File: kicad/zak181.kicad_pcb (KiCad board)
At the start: 4 copper layers, 215.3 x 92.7 mm, 119 parts, among them IC1 Z180, J1 JTAG, J10 DE15, J2 DB25_Receptacle_MountingHoles, J3 Compact Flash, J4 Speaker, J5 Keyboard, J7 DSUB-9, J8 USB C, J9 Reset, Q2 BC547, Q3 BC547, Q4 BC547, Q5 BC547, SW1 Reset, U17 LM386, U18 NE555P, U2 Z80 PIO A, U20 XC95108PC84, U21 74HC377, U22 74HC244, U23 27C64, U24 74HC166, U25 MAX232, U26 CH340N, U27 62256, U28 AS6C4008, U29 27C128, U3 AY-3-8912, U30 74HC377, U31 GAL16V8, U32 74HC157, U33 GAL16V8, U40 AS6C4008, U8 74HC138, X1 25.175 MHz, Y2 12.288 MHz

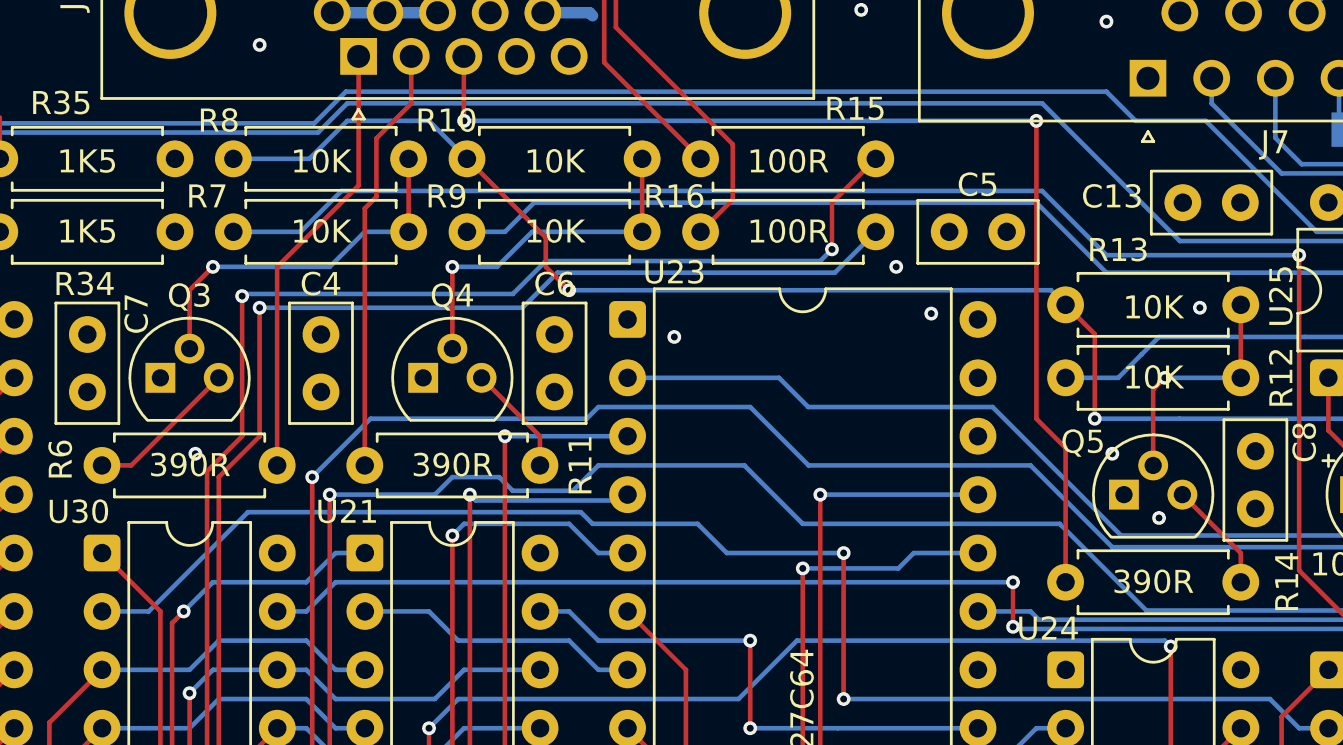
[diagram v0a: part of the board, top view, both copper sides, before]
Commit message: hw/vga: reduce resistance in DAC to impove image sharpness
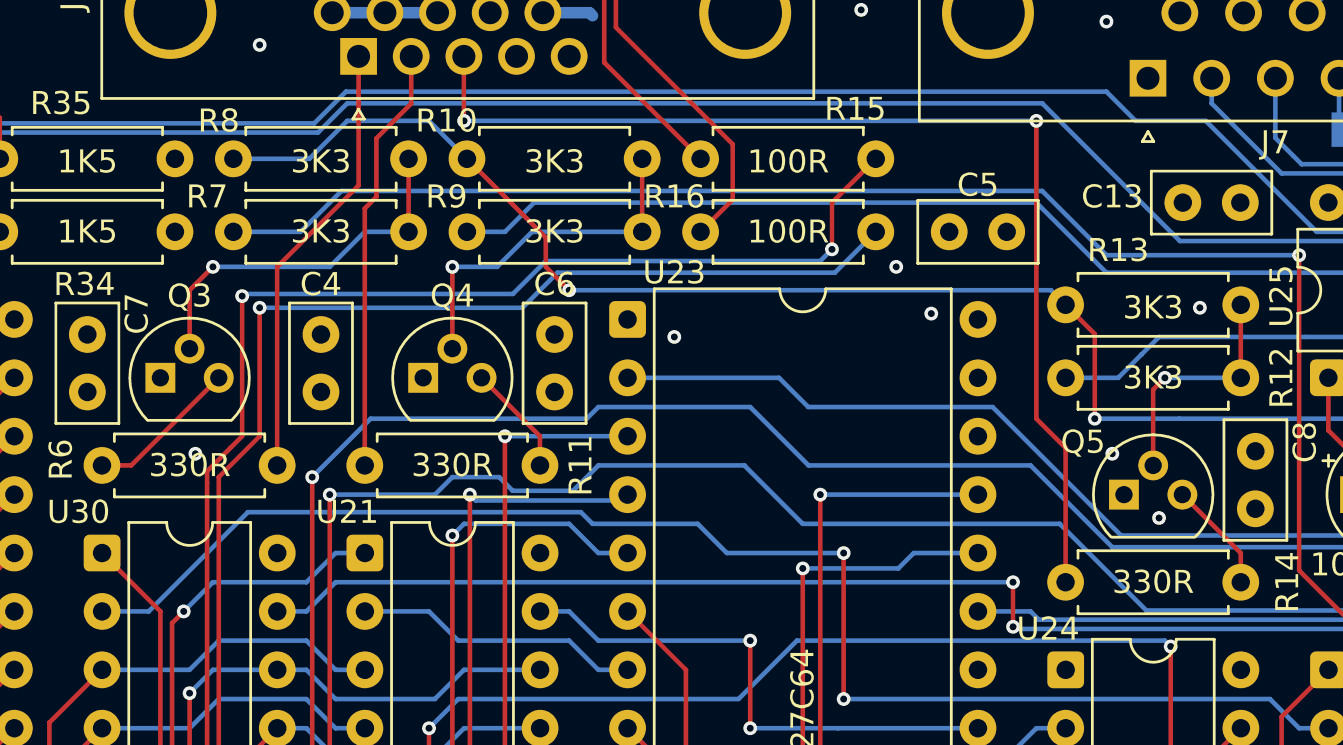
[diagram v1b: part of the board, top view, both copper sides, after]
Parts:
- R10, R12, R13, R7, R8, R9: value 10K -> 3K3
- R11, R14, R6: value 390R -> 330R
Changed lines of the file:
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@@
 			)
 		)
-		(property "Value" "390R"
+		(property "Value" "330R"
 			(at 3.81 0 0)
 			(layer "F.SilkS")
@@
 			)
 		)
-		(property "Value" "10K"
+		(property "Value" "3K3"
 			(at 3.81 0 0)
 			(layer "F.SilkS")
@@
 			)
 		)
-		(property "Value" "10K"
+		(property "Value" "3K3"
 			(at 3.81 0 0)
 			(layer "F.SilkS")
@@
 			)
 		)
-		(property "Value" "10K"
+		(property "Value" "3K3"
 			(at 3.81 0.127 0)
 			(layer "F.SilkS")
@@
 			)
 		)
-		(property "Value" "10K"
+		(property "Value" "3K3"
 			(at 3.81 0.127 0)
 			(layer "F.SilkS")
@@
 			)
 		)
-		(property "Value" "10K"
+		(property "Value" "3K3"
 			(at 3.81 0.127 0)
 			(layer "F.SilkS")
@@
 			)
 		)
-		(property "Value" "10K"
+		(property "Value" "3K3"
 			(at 3.81 0 0)
 			(layer "F.SilkS")
@@
 			)
 		)
-		(property "Value" "390R"
+		(property "Value" "330R"
 			(at 3.81 0 0)
 			(layer "F.SilkS")
@@
 			)
 		)
-		(property "Value" "390R"
+		(property "Value" "330R"
 			(at 3.815 0 0)
 			(layer "F.SilkS")
